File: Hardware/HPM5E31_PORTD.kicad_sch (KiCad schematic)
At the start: 1 part, among them U1 HPM5E31IGN1

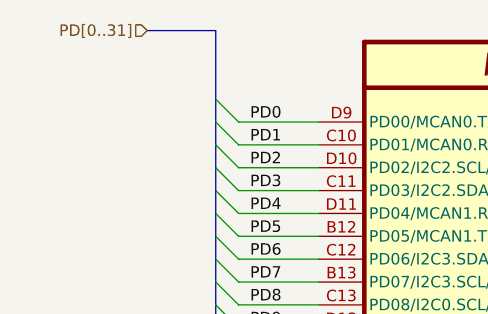
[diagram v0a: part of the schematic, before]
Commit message: 新增ESC IO引出，ESC CTR LED，EUI接口
编码器接口电源输出加保险，SPI加ESD
PY32ADC外部接口加ESD
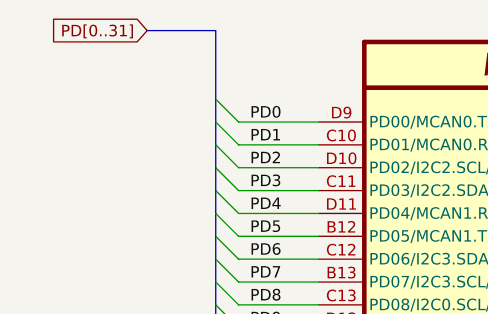
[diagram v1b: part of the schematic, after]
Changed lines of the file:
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@@
 		)
 	)
-	(hierarchical_label "PD[0..31]"
+	(global_label "PD[0..31]"
 		(shape input)
 		(at 71.12 43.18 180)
+		(fields_autoplaced yes)
 		(effects
 			(font
@@
 			(justify right)
 		)
+		(property "Intersheetrefs" "${INTERSHEET_REFS}"
+			(at 59.0633 43.18 0)
+			(effects
+				(font
+					(size 1.27 1.27)
+				)
+				(justify right)
+				(hide yes)
+			)
+		)
 	)

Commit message: 拉线
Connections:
- net PD0: now also U1.M2 (DCDC_IN); no longer U1.D9 (PD00/MCAN0.TXD/ESC0.GPI31/ESC0.GPO32/PPI0.DQ02/PWM0.P0/TRGM.P00/ESC0.REFCK/ESC0.CTR0)
- net PD1: no longer U1.C10 (PD01/MCAN0.RXD/ESC0.GPI30/ESC0.GPO33/PPI0.DQ03/PWM0.P1/TRGM.P01/ESC0.REFCK/ESC0.CTR1)
- net PD10: no longer U1.E12 (PD10/MCAN2.STBY/ESC0.GPI21/ESC0.GPO42/PPI0.CTR1/PWM1.P2/TRGM.P10)
- net PD11: no longer U1.E11 (PD11/ESC0.GPI20/ESC0.GPO43/PPI0.CS2/PWM1.P3/TRGM.P11)
- net PD12: no longer U1.F12 (PD12/I2C1.SDA/ESC0.GPI19/ESC0.GPO44/PPI0.DQ15/PWM1.P4/TRGM.P12)
- net PD13: no longer U1.F11 (PD13/I2C1.SCL/MCAN3.STBY/ESC0.GPI18/ESC0.GPO45/PPI0.DM1/PWM1.P5/TRGM.P13)
- net PD14: no longer U1.G14 (PD14/MCAN3.RXD/ESC0.GPI17/ESC0.GPO46/PPI0.DQ08/PWM1.P6/TRGM.P14/ESC0.REFCK/SYSCTL.CLK_OBS3)
- net PD15: no longer U1.G13 (PD15/MCAN3.TXD/ESC0.GPI16/ESC0.GPO47/PPI0.DM1/PWM1.P7/TRGM.P15/ESC0.REFCK/SYSCTL.CLK_OBS2)
- net PD16: no longer U1.G12 (PD16/ESC0.GPI15/ESC0.GPO48/PPI0.DQ10/ESC0.GPO00/SYSCTL.CLK_OBS0/ESC0.P2_RXDV)
- net PD17: no longer U1.H14 (PD17/ESC0.GPI14/ESC0.GPO49/PPI0.DQ09/ESC0.GPO01/SYSCTL.CLK_OBS1/ESC0.P2_RXD0)
- net PD18: no longer U1.H13 (PD18/ESC0.GPI13/ESC0.GPO50/PPI0.DQ12/ESC0.GPO02/ESC0.P2_RXD1)
- net PD19: no longer U1.H12 (PD19/ESC0.GPI12/ESC0.GPO51/PPI0.DQ11/ESC0.GPO03/ESC0.P2_RXD2)
- net PD2: no longer U1.D10 (PD02/I2C2.SCL/MCAN0.STBY/ESC0.GPI29/ESC0.GPO34/PPI0.DQ00/PWM0.P2/TRGM.P02/ESC0.SCL/QEI0.H1/EWDG1.RST/ESC0.CTR2)
- net PD20: no longer U1.J14 (PD20/ESC0.GPI11/ESC0.GPO52/PPI0.DQ14/ESC0.GPO04/ESC0.P2_RXD3)
- net PD21: no longer U1.J13 (PD21/ESC0.GPI10/ESC0.GPO53/PPI0.DQ13/ESC0.GPO05/QEO1.Z/ESC0.P2_RXCK)
- net PD22: no longer U1.J12 (PD22/ESC0.GPI09/ESC0.GPO54/PPI0.DQ15/ESC0.GPO06/QEO1.B/ESC0.P2_RXER)
- net PD23: no longer U1.F10 (PD23/ESC0.GPI08/ESC0.GPO55/PPI0.DM0/ESC0.GPO07/QEO1.A/ESC0.P2_TXCK)
- net PD24: no longer U1.G11 (PD24/ESC0.GPI07/ESC0.GPO56/PPI0.DQ06/ESC0.GPO08/SDM0.DAT3/ESC0.P2_TXD0)
- net PD25: no longer U1.G10 (PD25/ESC0.GPI06/ESC0.GPO57/PPI0.DQ07/ESC0.GPO09/SDM0.CLK3/OWR0.DAT/ESC0.P2_TXD1)
- net PD26: no longer U1.H11 (PD26/ESC0.GPI05/ESC0.GPO58/PPI0.DQ05/ESC0.GPO10/QEI1.H1/SDM0.CLK2/OWR1.DAT/ESC0.P2_TXD2)
- net PD27: no longer U1.H10 (PD27/ESC0.GPI04/ESC0.GPO59/PPI0.DQ04/ESC0.GPO11/QEI1.F/SDM0.DAT2/ESC0.P2_TXD3)
- net PD28: no longer U1.J11 (PD28/ESC0.GPI03/ESC0.GPO60/PPI0.DQ03/ESC0.GPO12/QEI1.H0/SDM0.CLK1/ESC0.P2_TXEN)
- net PD29: no longer U1.J10 (PD29/ESC0.GPI02/ESC0.GPO61/PPI0.DQ02/ESC0.GPO13/QEI1.Z/SDM0.DAT1/ESC0.REFCK)
- net PD3: now also U1.N2 (DCDC_LP); no longer U1.C11 (PD03/I2C2.SDA/MCAN1.STBY/ESC0.GPI28/ESC0.GPO35/PPI0.DQ01/PWM0.P3/TRGM.P03/ESC0.SDA/QEI0.F/ESC0.CTR3)
- net PD30: no longer U1.K12 (PD30/ESC0.GPI01/ESC0.GPO62/PPI0.DQ01/ESC0.GPO14/QEI1.A/SDM0.CLK0/ESC0.MDIO)
- net PD31: no longer U1.K11 (PD31/ESC0.GPI00/ESC0.GPO63/PPI0.DQ00/ESC0.GPO15/QEI1.B/SDM0.DAT0/ESC0.MDC)
- net PD4: now also U1.P3 (DCDC_LP); no longer U1.D11 (PD04/MCAN1.RXD/ESC0.GPI27/ESC0.GPO36/PPI0.DQ10/PWM0.P4/TRGM.P04/QEI0.H0/ESC0.CTR4)
- net PD5: no longer U1.B12 (PD05/MCAN1.TXD/ESC0.GPI26/ESC0.GPO37/PPI0.DQ13/PWM0.P5/TRGM.P05/QEI0.Z/QEO0.Z/ESC0.CTR5)
- net PD6: no longer U1.C12 (PD06/I2C3.SDA/ESC0.GPI25/ESC0.GPO38/PPI0.DQ14/PWM0.P6/TRGM.P06/QEI0.B/QEO0.B/ESC0.CTR6)
- net PD7: no longer U1.B13 (PD07/I2C3.SCL/ESC0.GPI24/ESC0.GPO39/PPI0.CTR3/PWM0.P7/TRGM.P07/QEI0.A/QEO0.A/ESC0.CTR7)
- net PD8: no longer U1.C13 (PD08/I2C0.SCL/MCAN2.TXD/ESC0.GPI23/ESC0.GPO40/PPI0.CS3/PWM1.P0/TRGM.P08/ESC0.SCL/ESC0.CTR8)
- net PD9: no longer U1.D12 (PD09/I2C0.SDA/MCAN2.RXD/ESC0.GPI22/ESC0.GPO41/PWM1.P1/TRGM.P09/ESC0.SDA)
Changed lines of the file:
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@@
 		(lib_id "HPM5E00_Library:HPM5E31IGN1")
 		(at 95.25 44.45 0)
-		(unit 7)
+		(unit 1)
 		(exclude_from_sim no)
 		(in_bom yes)
@@
 		(pin "L6"
 		)
-		(instances
-			(project "HPM5E31_ECatDualFOC"
-				(path "/a07e9810-3899-4327-ba8f-f24142a7c70e/b9a8d5a3-7d25-4818-87f6-adc719379948/e09544f5-80d9-4f28-9fde-22611ec0b45f"
-					(reference "U1")
-					(unit 7)
-				)
-			)
-		)
 	)

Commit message: 修存档拉线
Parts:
- renumbered U1 to U3
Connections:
- net PD0: now also U3.D9 (PD00/MCAN0.TXD/ESC0.GPI31/ESC0.GPO32/PPI0.DQ02/PWM0.P0/TRGM.P00/ESC0.REFCK/ESC0.CTR0); no longer U3.M2 (DCDC_IN)
- net PD1: now also U3.C10 (PD01/MCAN0.RXD/ESC0.GPI30/ESC0.GPO33/PPI0.DQ03/PWM0.P1/TRGM.P01/ESC0.REFCK/ESC0.CTR1)
- net PD10: now also U3.E12 (PD10/MCAN2.STBY/ESC0.GPI21/ESC0.GPO42/PPI0.CTR1/PWM1.P2/TRGM.P10)
- net PD11: now also U3.E11 (PD11/ESC0.GPI20/ESC0.GPO43/PPI0.CS2/PWM1.P3/TRGM.P11)
- net PD12: now also U3.F12 (PD12/I2C1.SDA/ESC0.GPI19/ESC0.GPO44/PPI0.DQ15/PWM1.P4/TRGM.P12)
- net PD13: now also U3.F11 (PD13/I2C1.SCL/MCAN3.STBY/ESC0.GPI18/ESC0.GPO45/PPI0.DM1/PWM1.P5/TRGM.P13)
- net PD14: now also U3.G14 (PD14/MCAN3.RXD/ESC0.GPI17/ESC0.GPO46/PPI0.DQ08/PWM1.P6/TRGM.P14/ESC0.REFCK/SYSCTL.CLK_OBS3)
- net PD15: now also U3.G13 (PD15/MCAN3.TXD/ESC0.GPI16/ESC0.GPO47/PPI0.DM1/PWM1.P7/TRGM.P15/ESC0.REFCK/SYSCTL.CLK_OBS2)
- net PD16: now also U3.G12 (PD16/ESC0.GPI15/ESC0.GPO48/PPI0.DQ10/ESC0.GPO00/SYSCTL.CLK_OBS0/ESC0.P2_RXDV)
- net PD17: now also U3.H14 (PD17/ESC0.GPI14/ESC0.GPO49/PPI0.DQ09/ESC0.GPO01/SYSCTL.CLK_OBS1/ESC0.P2_RXD0)
- net PD18: now also U3.H13 (PD18/ESC0.GPI13/ESC0.GPO50/PPI0.DQ12/ESC0.GPO02/ESC0.P2_RXD1)
- net PD19: now also U3.H12 (PD19/ESC0.GPI12/ESC0.GPO51/PPI0.DQ11/ESC0.GPO03/ESC0.P2_RXD2)
- net PD2: now also U3.D10 (PD02/I2C2.SCL/MCAN0.STBY/ESC0.GPI29/ESC0.GPO34/PPI0.DQ00/PWM0.P2/TRGM.P02/ESC0.SCL/QEI0.H1/EWDG1.RST/ESC0.CTR2)
- net PD20: now also U3.J14 (PD20/ESC0.GPI11/ESC0.GPO52/PPI0.DQ14/ESC0.GPO04/ESC0.P2_RXD3)
- net PD21: now also U3.J13 (PD21/ESC0.GPI10/ESC0.GPO53/PPI0.DQ13/ESC0.GPO05/QEO1.Z/ESC0.P2_RXCK)
- net PD22: now also U3.J12 (PD22/ESC0.GPI09/ESC0.GPO54/PPI0.DQ15/ESC0.GPO06/QEO1.B/ESC0.P2_RXER)
- net PD23: now also U3.F10 (PD23/ESC0.GPI08/ESC0.GPO55/PPI0.DM0/ESC0.GPO07/QEO1.A/ESC0.P2_TXCK)
- net PD24: now also U3.G11 (PD24/ESC0.GPI07/ESC0.GPO56/PPI0.DQ06/ESC0.GPO08/SDM0.DAT3/ESC0.P2_TXD0)
- net PD25: now also U3.G10 (PD25/ESC0.GPI06/ESC0.GPO57/PPI0.DQ07/ESC0.GPO09/SDM0.CLK3/OWR0.DAT/ESC0.P2_TXD1)
- net PD26: now also U3.H11 (PD26/ESC0.GPI05/ESC0.GPO58/PPI0.DQ05/ESC0.GPO10/QEI1.H1/SDM0.CLK2/OWR1.DAT/ESC0.P2_TXD2)
- net PD27: now also U3.H10 (PD27/ESC0.GPI04/ESC0.GPO59/PPI0.DQ04/ESC0.GPO11/QEI1.F/SDM0.DAT2/ESC0.P2_TXD3)
- net PD28: now also U3.J11 (PD28/ESC0.GPI03/ESC0.GPO60/PPI0.DQ03/ESC0.GPO12/QEI1.H0/SDM0.CLK1/ESC0.P2_TXEN)
- net PD29: now also U3.J10 (PD29/ESC0.GPI02/ESC0.GPO61/PPI0.DQ02/ESC0.GPO13/QEI1.Z/SDM0.DAT1/ESC0.REFCK)
- net PD3: now also U3.C11 (PD03/I2C2.SDA/MCAN1.STBY/ESC0.GPI28/ESC0.GPO35/PPI0.DQ01/PWM0.P3/TRGM.P03/ESC0.SDA/QEI0.F/ESC0.CTR3); no longer U3.N2 (DCDC_LP)
- net PD30: now also U3.K12 (PD30/ESC0.GPI01/ESC0.GPO62/PPI0.DQ01/ESC0.GPO14/QEI1.A/SDM0.CLK0/ESC0.MDIO)
- net PD31: now also U3.K11 (PD31/ESC0.GPI00/ESC0.GPO63/PPI0.DQ00/ESC0.GPO15/QEI1.B/SDM0.DAT0/ESC0.MDC)
- net PD4: now also U3.D11 (PD04/MCAN1.RXD/ESC0.GPI27/ESC0.GPO36/PPI0.DQ10/PWM0.P4/TRGM.P04/QEI0.H0/ESC0.CTR4); no longer U3.P3 (DCDC_LP)
- net PD5: now also U3.B12 (PD05/MCAN1.TXD/ESC0.GPI26/ESC0.GPO37/PPI0.DQ13/PWM0.P5/TRGM.P05/QEI0.Z/QEO0.Z/ESC0.CTR5)
- net PD6: now also U3.C12 (PD06/I2C3.SDA/ESC0.GPI25/ESC0.GPO38/PPI0.DQ14/PWM0.P6/TRGM.P06/QEI0.B/QEO0.B/ESC0.CTR6)
- net PD7: now also U3.B13 (PD07/I2C3.SCL/ESC0.GPI24/ESC0.GPO39/PPI0.CTR3/PWM0.P7/TRGM.P07/QEI0.A/QEO0.A/ESC0.CTR7)
- net PD8: now also U3.C13 (PD08/I2C0.SCL/MCAN2.TXD/ESC0.GPI23/ESC0.GPO40/PPI0.CS3/PWM1.P0/TRGM.P08/ESC0.SCL/ESC0.CTR8)
- net PD9: now also U3.D12 (PD09/I2C0.SDA/MCAN2.RXD/ESC0.GPI22/ESC0.GPO41/PWM1.P1/TRGM.P09/ESC0.SDA)
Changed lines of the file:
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@@
 		(lib_id "HPM5E00_Library:HPM5E31IGN1")
 		(at 95.25 44.45 0)
-		(unit 1)
+		(unit 7)
 		(exclude_from_sim no)
 		(in_bom yes)
@@
 		(dnp no)
 		(fields_autoplaced yes)
-		(property "Reference" "U1"
+		(property "Reference" "U3"
 			(at 227.33 89.5349 0)
 			(effects
@@
 		(pin "L6"
 		)
+		(instances
+			(project "HPM5E31_ECatDualFOC"
+				(path "/a07e9810-3899-4327-ba8f-f24142a7c70e/b9a8d5a3-7d25-4818-87f6-adc719379948/e09544f5-80d9-4f28-9fde-22611ec0b45f"
+					(reference "U3")
+					(unit 7)
+				)
+			)
+		)
 	)
